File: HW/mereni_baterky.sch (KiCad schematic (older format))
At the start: 2 parts

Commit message: fix mistake
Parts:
- R? (x2): footprint (none) -> Resistor_SMD:R_0402_1005Metric
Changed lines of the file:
@@
 F 0 "R?" H 6770 2946 50  0000 L CNN
 F 1 "39k" H 6770 2855 50  0000 L CNN
-F 2 "" V 6630 2900 50  0001 C CNN
+F 2 "Resistor_SMD:R_0402_1005Metric" V 6630 2900 50  0001 C CNN
 F 3 "~" H 6700 2900 50  0001 C CNN
 	1    6700 2900
@@
 F 0 "R?" H 6770 3596 50  0000 L CNN
 F 1 "10k" H 6770 3505 50  0000 L CNN
-F 2 "" V 6630 3550 50  0001 C CNN
+F 2 "Resistor_SMD:R_0402_1005Metric" V 6630 3550 50  0001 C CNN
 F 3 "~" H 6700 3550 50  0001 C CNN
 	1    6700 3550

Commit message: add some codes for JLCPCB, change package and schematic of CP2102
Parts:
- R?: LCSC (none) -> C25783
- R?: LCSC (none) -> C25744
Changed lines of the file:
@@
 F 2 "Resistor_SMD:R_0402_1005Metric" V 6630 2900 50  0001 C CNN
 F 3 "~" H 6700 2900 50  0001 C CNN
+F 4 "C25783" H 6700 2900 50  0001 C CNN "LCSC"
 	1    6700 2900
 	1    0    0    -1
@@
 F 2 "Resistor_SMD:R_0402_1005Metric" V 6630 3550 50  0001 C CNN
 F 3 "~" H 6700 3550 50  0001 C CNN
+F 4 "C25744" H 6700 3550 50  0001 C CNN "LCSC"
 	1    6700 3550
 	1    0    0    -1

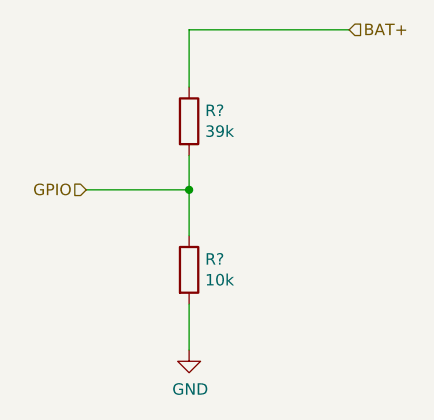
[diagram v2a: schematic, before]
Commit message: numbering components, place components on board
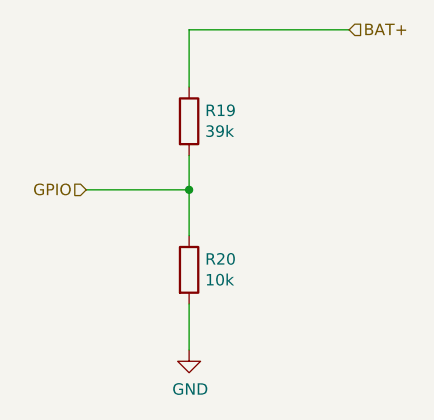
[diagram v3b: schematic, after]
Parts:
- gave numbers to parts that had none: 2
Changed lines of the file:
@@
 $EndDescr
 $Comp
-L Device:R R?
+L Device:R R19
 U 1 1 5F7D9288
 P 6700 2900
-F 0 "R?" H 6770 2946 50  0000 L CNN
+F 0 "R19" H 6770 2946 50  0000 L CNN
 F 1 "39k" H 6770 2855 50  0000 L CNN
 F 2 "Resistor_SMD:R_0402_1005Metric" V 6630 2900 50  0001 C CNN
@@
 $EndComp
 $Comp
-L Device:R R?
+L Device:R R20
 U 1 1 5F7D9363
 P 6700 3550
-F 0 "R?" H 6770 3596 50  0000 L CNN
+F 0 "R20" H 6770 3596 50  0000 L CNN
 F 1 "10k" H 6770 3505 50  0000 L CNN
 F 2 "Resistor_SMD:R_0402_1005Metric" V 6630 3550 50  0001 C CNN
@@
 	6700 3700 6700 3900
 $Comp
-L power:GND #PWR?
+L power:GND #PWR0315
 U 1 1 5F7D9637
 P 6700 3900
-F 0 "#PWR?" H 6700 3650 50  0001 C CNN
+F 0 "#PWR0315" H 6700 3650 50  0001 C CNN
 F 1 "GND" H 6705 3727 50  0000 C CNN
 F 2 "" H 6700 3900 50  0001 C CNN
